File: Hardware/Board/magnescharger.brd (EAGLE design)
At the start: 81.8 x 54.5 mm, 18 parts, among them IC1 LM324N, U1 MCP2551P

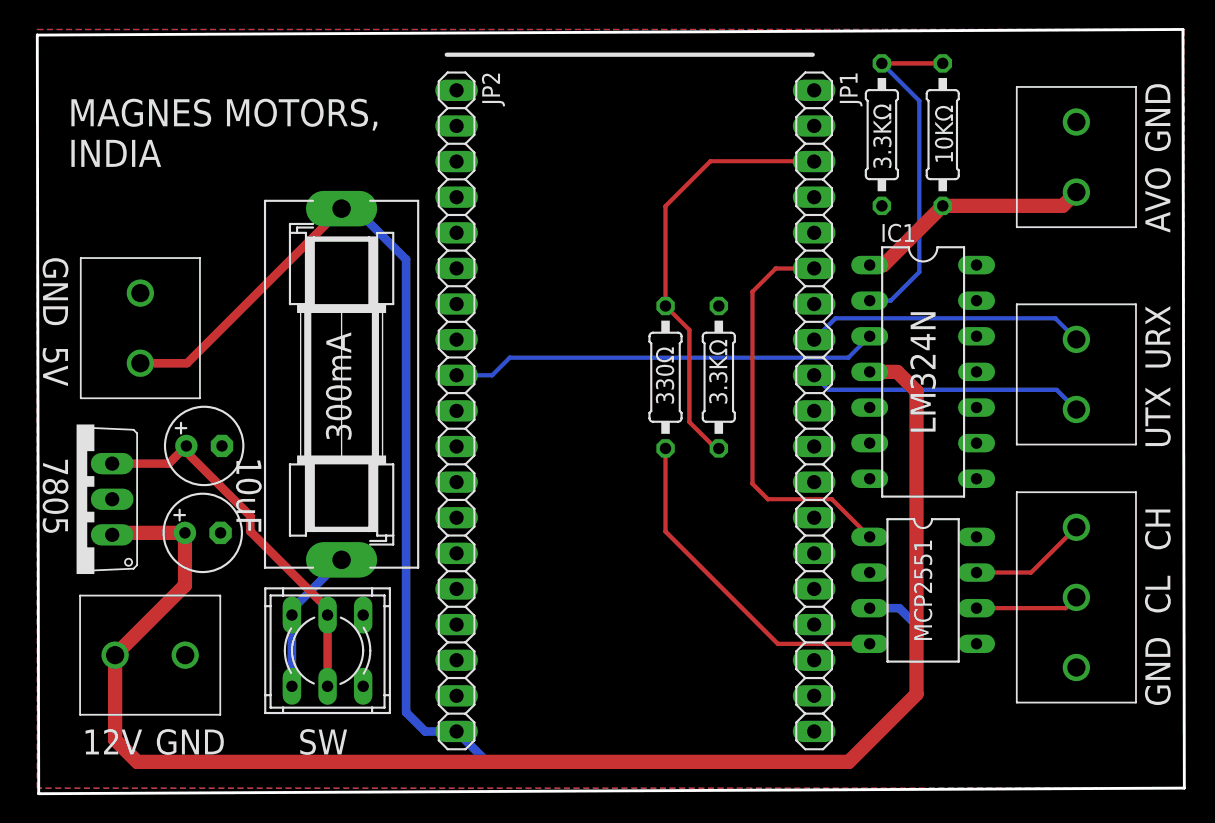
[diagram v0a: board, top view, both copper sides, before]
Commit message: added mounting holes
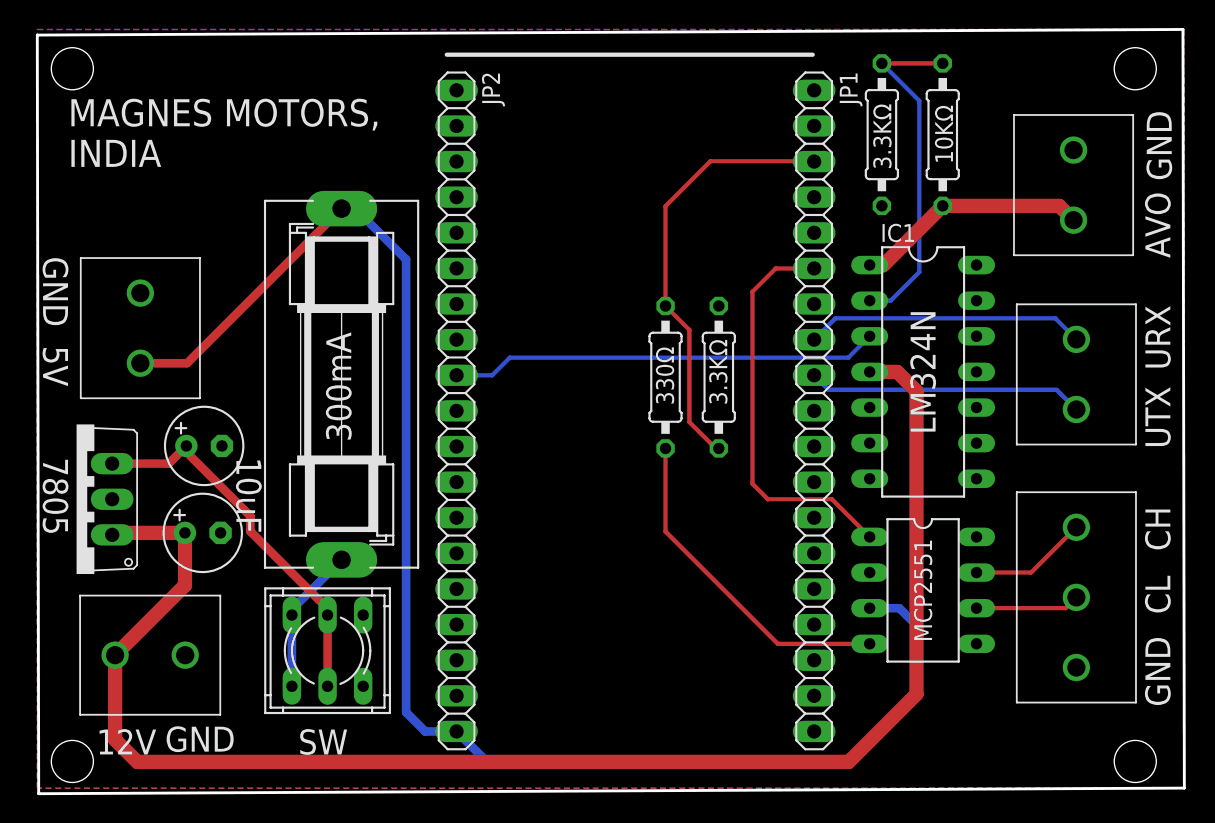
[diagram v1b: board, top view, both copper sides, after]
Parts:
- moved OUTPUT 2.01 mm to (69.4, 41.5)
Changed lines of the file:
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@@
 <layer number="43" name="vRestrict" color="2" fill="10" visible="yes" active="yes"/>
 <layer number="44" name="Drills" color="7" fill="1" visible="no" active="yes"/>
-<layer number="45" name="Holes" color="7" fill="1" visible="no" active="yes"/>
+<layer number="45" name="Holes" color="7" fill="1" visible="yes" active="yes"/>
 <layer number="46" name="Milling" color="3" fill="1" visible="no" active="yes"/>
 <layer number="47" name="Measures" color="7" fill="1" visible="no" active="yes"/>
@@
 <text x="-3.2" y="28.6" size="1.778" layer="25" rot="SR270" align="center">5V</text>
 <text x="-3.2" y="19.3" size="1.778" layer="25" rot="SR270" align="center">7805</text>
-<text x="-1.3" y="0.9" size="1.778" layer="25">12V</text>
-<text x="3.9" y="0.9" size="1.778" layer="25">GND</text>
+<text x="-0.3" y="0.9" size="1.778" layer="25">12V</text>
+<text x="4.6" y="1.1" size="1.778" layer="25">GND</text>
 <text x="14.1" y="0.9" size="1.778" layer="25">SW</text>
 <text x="40.9" y="25.8" size="1.27" layer="25" rot="R90">330Ω</text>
@@
 <text x="76.3" y="22.7" size="1.778" layer="25" rot="R90">UTX</text>
 <text x="76.3" y="28.3" size="1.778" layer="25" rot="R90">URX</text>
-<text x="76.3" y="38.1" size="1.778" layer="25" rot="R270" align="top-right">AVO</text>
-<text x="76.3" y="43.8" size="1.778" layer="25" rot="R270" align="top-right">GND</text>
+<text x="76.3" y="36.3" size="1.778" layer="25" rot="R270" align="top-right">AVO</text>
+<text x="76.4" y="41.8" size="1.778" layer="25" rot="R270" align="top-right">GND</text>
 <text x="76.3" y="4.3" size="1.778" layer="25" rot="R270" align="top-right">GND</text>
 <text x="76.3" y="15.4" size="1.778" layer="25" rot="R90">CH</text>
@@
 <dimension x1="-4.5" y1="52.6" x2="77.3" y2="52.6" x3="36.4" y3="54.5" textsize="1.778" layer="25"/>
 <dimension x1="77.3" y1="52.6" x2="77.3" y2="-1.5" x3="80.4" y3="25.55" textsize="1.778" layer="25" dtype="vertical"/>
+<hole x="-2" y="49.8" drill="3"/>
+<hole x="-2" y="0.4" drill="3"/>
+<hole x="73.8" y="0.4" drill="3"/>
+<hole x="73.8" y="49.8" drill="3"/>
 </plain>
 <attributes>
@@
 <attribute name="VALUE" x="22.225" y="49.53" size="1.27" layer="27" rot="R270"/>
 </element>
-<element name="OUTPUT" library="Wurth_Elektronik_Electromechanic_Terminal_Blocks_Connectors_rev17a" library_urn="urn:adsk.eagle:library:485" package="691131710002" value="" x="69.6" y="43.5" smashed="yes" rot="R270">
-<attribute name="VALUE" x="63.322" y="46.75" size="1.27" layer="27" rot="R270"/>
+<element name="OUTPUT" library="Wurth_Elektronik_Electromechanic_Terminal_Blocks_Connectors_rev17a" library_urn="urn:adsk.eagle:library:485" package="691131710002" value="" x="69.4" y="41.5" smashed="yes" rot="R270">
+<attribute name="VALUE" x="63.122" y="44.75" size="1.27" layer="27" rot="R270"/>
 </element>
 <element name="POWER" library="Wurth_Elektronik_Electromechanic_Terminal_Blocks_Connectors_rev17a" library_urn="urn:adsk.eagle:library:485" package="691131710002" value="" x="3.55" y="7.98" smashed="yes">
@@
 <wire x1="54.86" y1="35.8" x2="55.85" y2="35.8" width="1.016" layer="1"/>
 <wire x1="55.85" y1="35.8" x2="60.07" y2="40.02" width="1.016" layer="1"/>
-<wire x1="60.07" y1="40.02" x2="68.62" y2="40.02" width="1.016" layer="1"/>
-<wire x1="68.62" y1="40.02" x2="69.6" y2="41" width="1.016" layer="1"/>
+<wire x1="60.07" y1="40.02" x2="68.38" y2="40.02" width="1.016" layer="1"/>
+<wire x1="68.38" y1="40.02" x2="69.4" y2="39" width="1.016" layer="1"/>
 </signal>
 <signal name="N$6">
